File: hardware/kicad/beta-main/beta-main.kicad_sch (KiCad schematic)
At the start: 7 parts

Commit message: add modifications
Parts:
- added J1: AUDIO, Connector_JST:JST_PH_B2B-PH-K_1x02_P2.00mm_Vertical, symbol Connector:Conn_01x02_Socket
- added J2: USB3-0, Connector_JST:JST_PH_B8B-PH-K_1x08_P2.00mm_Vertical, symbol Connector:Conn_01x08_Pin
- added J21: PWR, Connector_JST:JST_PH_B2B-PH-K_1x02_P2.00mm_Vertical, symbol Connector:Conn_01x02_Pin
- added J3, J4, J7: USB3-1, Connector_JST:JST_PH_B8B-PH-K_1x08_P2.00mm_Vertical, symbol Connector:Conn_01x08_Pin
- added J5: DSI, Connector_FFC-FPC:TE_1-84953-5_1x15-1MP_P1.0mm_Horizontal, symbol Connector:Conn_01x15_Socket
- added J6, J9: USB3_A, BETA:22009L012N1, symbol Connector:USB3_A
- added J8: CSI, Connector_FFC-FPC:TE_1-84953-5_1x15-1MP_P1.0mm_Horizontal, symbol Connector:Conn_01x15_Socket
- added MH10, MH11, MH12, MH9: M2.5, MountingHole:MountingHole_2.7mm_Pad, symbol Mechanical:MountingHole_Pad
- added U1: MAX98357A, Package_DFN_QFN:TQFN-16-1EP_3x3mm_P0.5mm_EP1.23x1.23mm, symbol Beta:MAX98357A
- renumbered MH2 to MH3, MH3 to MH5, MH4 to MH7
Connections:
- net GND: now also J2.8 (Pin_8), J21.2 (Pin_2), J3.8 (Pin_8), J5.1 (Pin_1), J5.10 (Pin_10), J5.13 (Pin_13), J5.4 (Pin_4), J5.7 (Pin_7), J8.1 (Pin_1), J8.10 (Pin_10), J8.4 (Pin_4), J8.7 (Pin_7), MH10.1, MH11.1, MH12.1, MH9.1, U1.11 (GND), U1.15 (GND), U1.17 (PAD), U1.3 (GND)
- new net: J1.2 (Pin_2), U1.10 (OUTN)
- new net: J1.1 (Pin_1), U1.9 (OUTP)
- new net: J4.1 (Pin_1), J6.1 (VBUS)
- new net: J4.2 (Pin_2), J6.2 (D-)
- new net: J4.3 (Pin_3), J6.3 (D+)
- new net: J4.4 (Pin_4), J6.5 (SSRX-)
- new net: J4.5 (Pin_5), J6.6 (SSRX+)
- new net: J4.6 (Pin_6), J6.8 (SSTX-)
- new net: J4.7 (Pin_7), J6.9 (SSTX+)
- new net: J4.8 (Pin_8), J6.10 (SHIELD), J6.4 (GND), J6.7 (DRAIN)
- new net: J7.1 (Pin_1), J9.1 (VBUS)
- new net: J7.8 (Pin_8), J9.10 (SHIELD), J9.4 (GND), J9.7 (DRAIN)
- new net: J7.2 (Pin_2), J9.2 (D-)
- new net: J7.3 (Pin_3), J9.3 (D+)
- new net: J7.4 (Pin_4), J9.5 (SSRX-)
- new net: J7.5 (Pin_5), J9.6 (SSRX+)
- new net: J7.6 (Pin_6), J9.8 (SSTX-)
- new net: J7.7 (Pin_7), J9.9 (SSTX+)
- new net +3V3: J5.14 (Pin_14), J5.15 (Pin_15), J8.15 (Pin_15), U1.2 (GAIN_SLOT), U1.4 (~{SD_MODE}), U1.7 (VDD), U1.8 (VDD)
- new net CAM_GPIO0: J8.11 (Pin_11)
- new net CAM_GPIO1: J8.12 (Pin_12)
- new net GPIO/PWR_BUT: J21.1 (Pin_1)
- new net High Speed Serial/USB3-0-D_N: J2.2 (Pin_2)
- new net High Speed Serial/USB3-0-D_P: J2.3 (Pin_3)
- new net High Speed Serial/USB3-0-RX_N: J2.4 (Pin_4)
- new net High Speed Serial/USB3-0-RX_P: J2.5 (Pin_5)
- new net High Speed Serial/USB3-0-TX_N: J2.6 (Pin_6)
- new net High Speed Serial/USB3-0-TX_P: J2.7 (Pin_7)
- new net High Speed Serial/USB3-1-D_N: J3.2 (Pin_2)
- new net High Speed Serial/USB3-1-D_P: J3.3 (Pin_3)
- new net High Speed Serial/USB3-1-RX_N: J3.4 (Pin_4)
- new net High Speed Serial/USB3-1-RX_P: J3.5 (Pin_5)
- new net High Speed Serial/USB3-1-TX_N: J3.6 (Pin_6)
- new net High Speed Serial/USB3-1-TX_P: J3.7 (Pin_7)
- new net I2S0_SCLK: U1.16 (BCLK)
- new net I2S0_SDO: U1.1 (DIN)
- new net I2S0_WS: U1.14 (LRCLK)
- new net MIPI0_C_N: J5.5 (Pin_5)
- new net MIPI0_C_P: J5.6 (Pin_6)
- new net MIPI0_D0_N: J5.8 (Pin_8)
- new net MIPI0_D0_P: J5.9 (Pin_9)
- new net MIPI0_D1_N: J5.2 (Pin_2)
- new net MIPI0_D1_P: J5.3 (Pin_3)
- new net MIPI1_C_N: J8.8 (Pin_8)
- new net MIPI1_C_P: J8.9 (Pin_9)
- new net MIPI1_D0_N: J8.2 (Pin_2)
- new net MIPI1_D0_P: J8.3 (Pin_3)
- new net MIPI1_D1_N: J8.5 (Pin_5)
- new net MIPI1_D1_P: J8.6 (Pin_6)
- new net SCL0: J5.11 (Pin_11)
- new net SCL1: J8.13 (Pin_13)
- new net SDA0: J5.12 (Pin_12)
- new net SDA1: J8.14 (Pin_14)
- new net VBUS: J2.1 (Pin_1), J3.1 (Pin_1)
- no-connect marks 0 -> 8
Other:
- removed sheet CM5
- added sheet GPIO (gpio.kicad_sch)
- added sheet High Speed Serial (high-speed-serial.kicad_sch)
- added sheet Peripherals (peripherals.kicad_sch)
- sheet PSU ports: added VBUS_EN; removed none
- note added: "A_OUT"
- note added: "Audio Interface"
- note added: "BNO"
- note added: "BOARD MOUNT"
- note added: "CSI"
- note added: "DISPLAY MOUNT"
- note added: "DSI"
- note added: "GPIO"
- note added: "HIGH SPEED"
- note added: "MIPI"
- note added: "MISC"
- note added: "SERVO"
- note added: "USB"
- note added: "USB 3.0"
- title: BETA MAIN BOARD -> BETA MAIN BOARD - CM5
- moved on the sheet: FID1, FID2, FID3, MH1, MH3, MH5, MH7

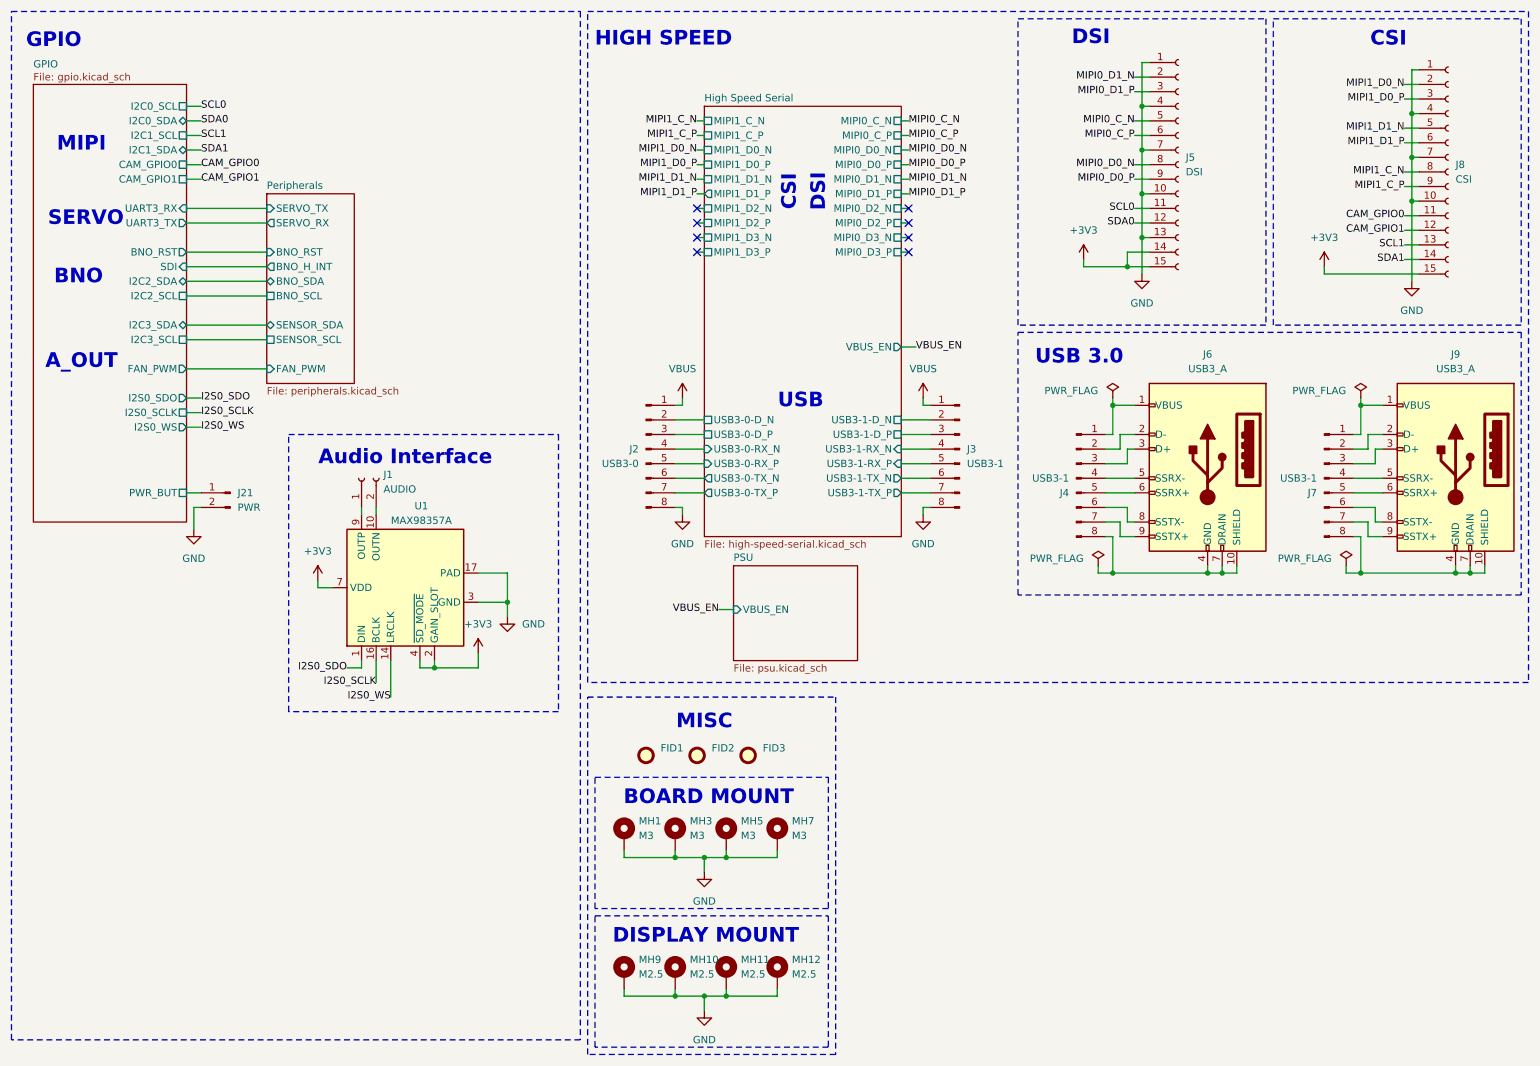
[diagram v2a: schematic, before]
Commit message: BOM, all easily found parts from digi
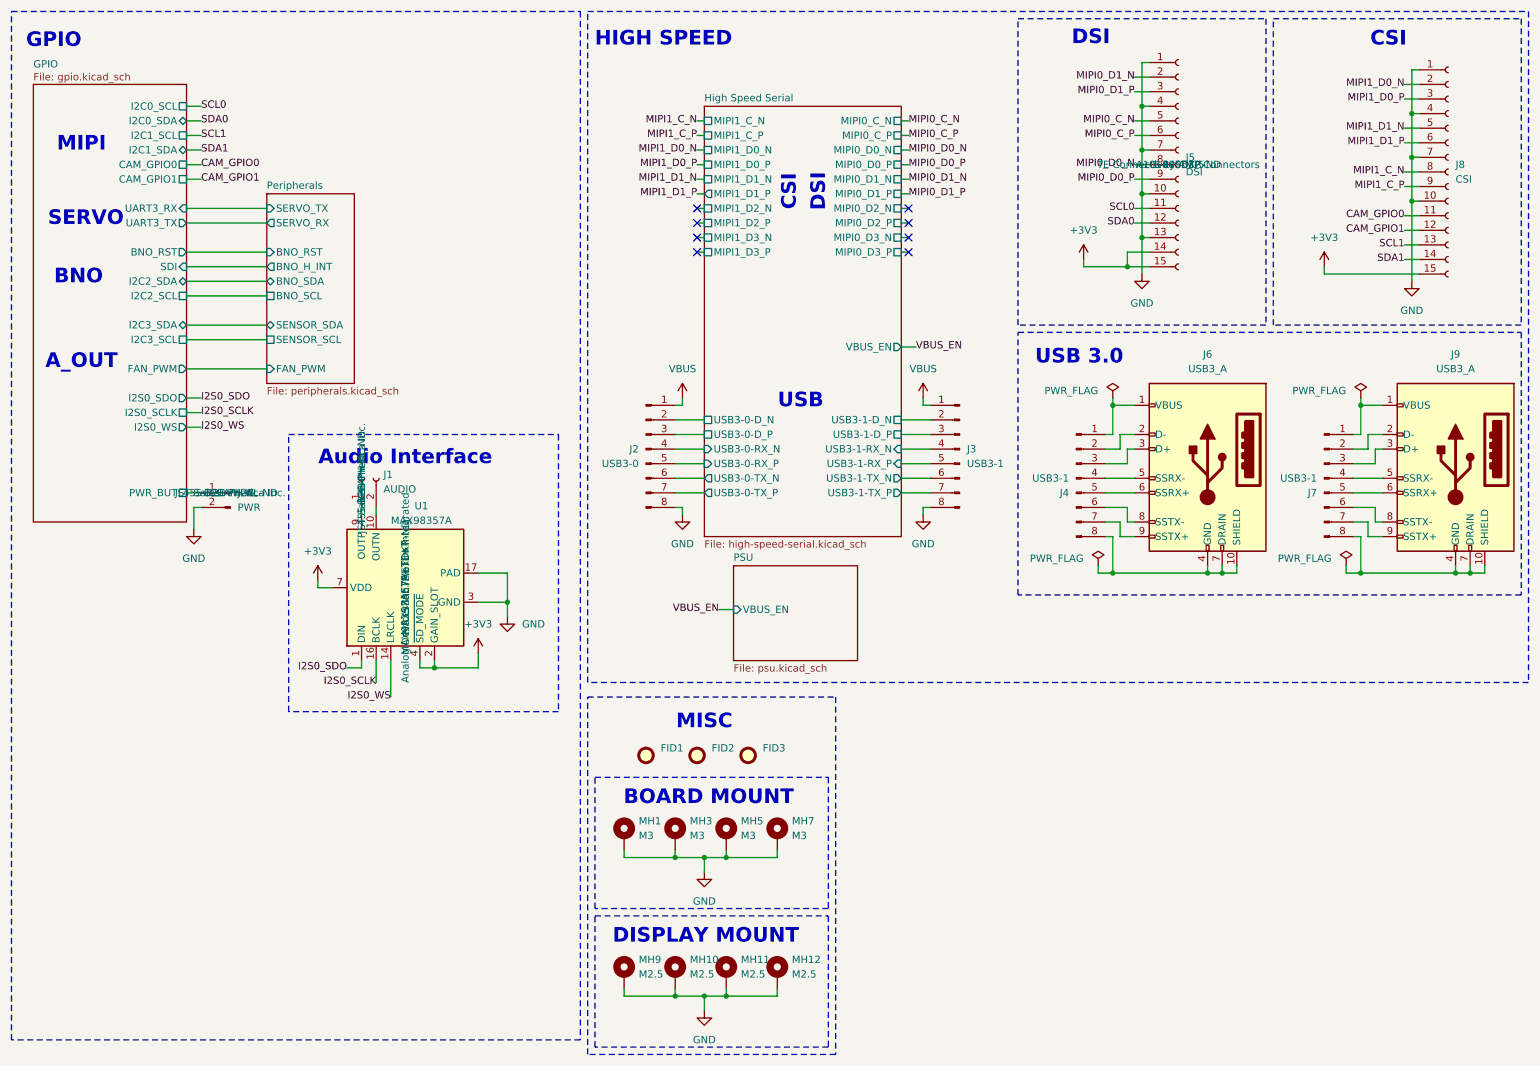
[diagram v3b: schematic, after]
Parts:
- J1, J21: DigiKey_Part_Number (none) -> 455-B2B-PH-KL-ND; MANUFACTURER (none) -> JST Sales America Inc.; MP (none) -> B2B-PH-KL
- J5: DigiKey_Part_Number (none) -> A101405DKR-ND; MANUFACTURER (none) -> TE Connectivity AMP Connectors; MP (none) -> 1-84953-5
- U1: DigiKey_Part_Number (none) -> MAX98357AETE+TDKR-ND; MANUFACTURER (none) -> Analog Devices Inc./Maxim Integrated; MP (none) -> MAX98357AETE+T
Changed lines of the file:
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@@
+			)
+		)
+		(property "DigiKey_Part_Number" "MAX98357AETE+TDKR-ND"
+			(at 81.28 114.3 0)
+			(effects
+				(font
+					(size 1.27 1.27)
+				)
+			)
+		)
+		(property "MANUFACTURER" "Analog Devices Inc./Maxim Integrated"
+			(at 81.28 114.3 0)
+			(effects
+				(font
+					(size 1.27 1.27)
+				)
+			)
+		)
+		(property "MP" "MAX98357AETE+T"
+			(at 81.28 114.3 0)
+			(effects
+				(font
+					(size 1.27 1.27)
+				)
 			)
 		)
@@
 			)
 		)
+		(property "DigiKey_Part_Number" "455-B2B-PH-KL-ND"
+			(at 73.66 95.25 0)
+			(effects
+				(font
+					(size 1.27 1.27)
+				)
+			)
+		)
+		(property "MANUFACTURER" "JST Sales America Inc."
+			(at 73.66 95.25 0)
+			(effects
+				(font
+					(size 1.27 1.27)
+				)
+			)
+		)
+		(property "MP" "B2B-PH-KL"
+			(at 73.66 95.25 0)
+			(effects
+				(font
+					(size 1.27 1.27)
+				)
+			)
+		)
 		(pin "2"
 		)
@@
 			)
 		)
+		(property "DigiKey_Part_Number" "455-B2B-PH-KL-ND"
+			(at 50.8 97.79 0)
+			(effects
+				(font
+					(size 1.27 1.27)
+				)
+			)
+		)
+		(property "MANUFACTURER" "JST Sales America Inc."
+			(at 50.8 97.79 0)
+			(effects
+				(font
+					(size 1.27 1.27)
+				)
+			)
+		)
+		(property "MP" "B2B-PH-KL"
+			(at 50.8 97.79 0)
+			(effects
+				(font
+					(size 1.27 1.27)
+				)
+			)
+		)
 		(pin "2"
 		)
@@
 			)
 		)
+		(property "DigiKey_Part_Number" "A101405DKR-ND"
+			(at 215.9 40.64 0)
+			(effects
+				(font
+					(size 1.27 1.27)
+				)
+			)
+		)
+		(property "MANUFACTURER" "TE Connectivity AMP Connectors"
+			(at 215.9 40.64 0)
+			(effects
+				(font
+					(size 1.27 1.27)
+				)
+			)
+		)
+		(property "MP" "1-84953-5"
+			(at 215.9 40.64 0)
+			(effects
+				(font
+					(size 1.27 1.27)
+				)
+			)
+		)

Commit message: resolve DRC issues and generate fab files
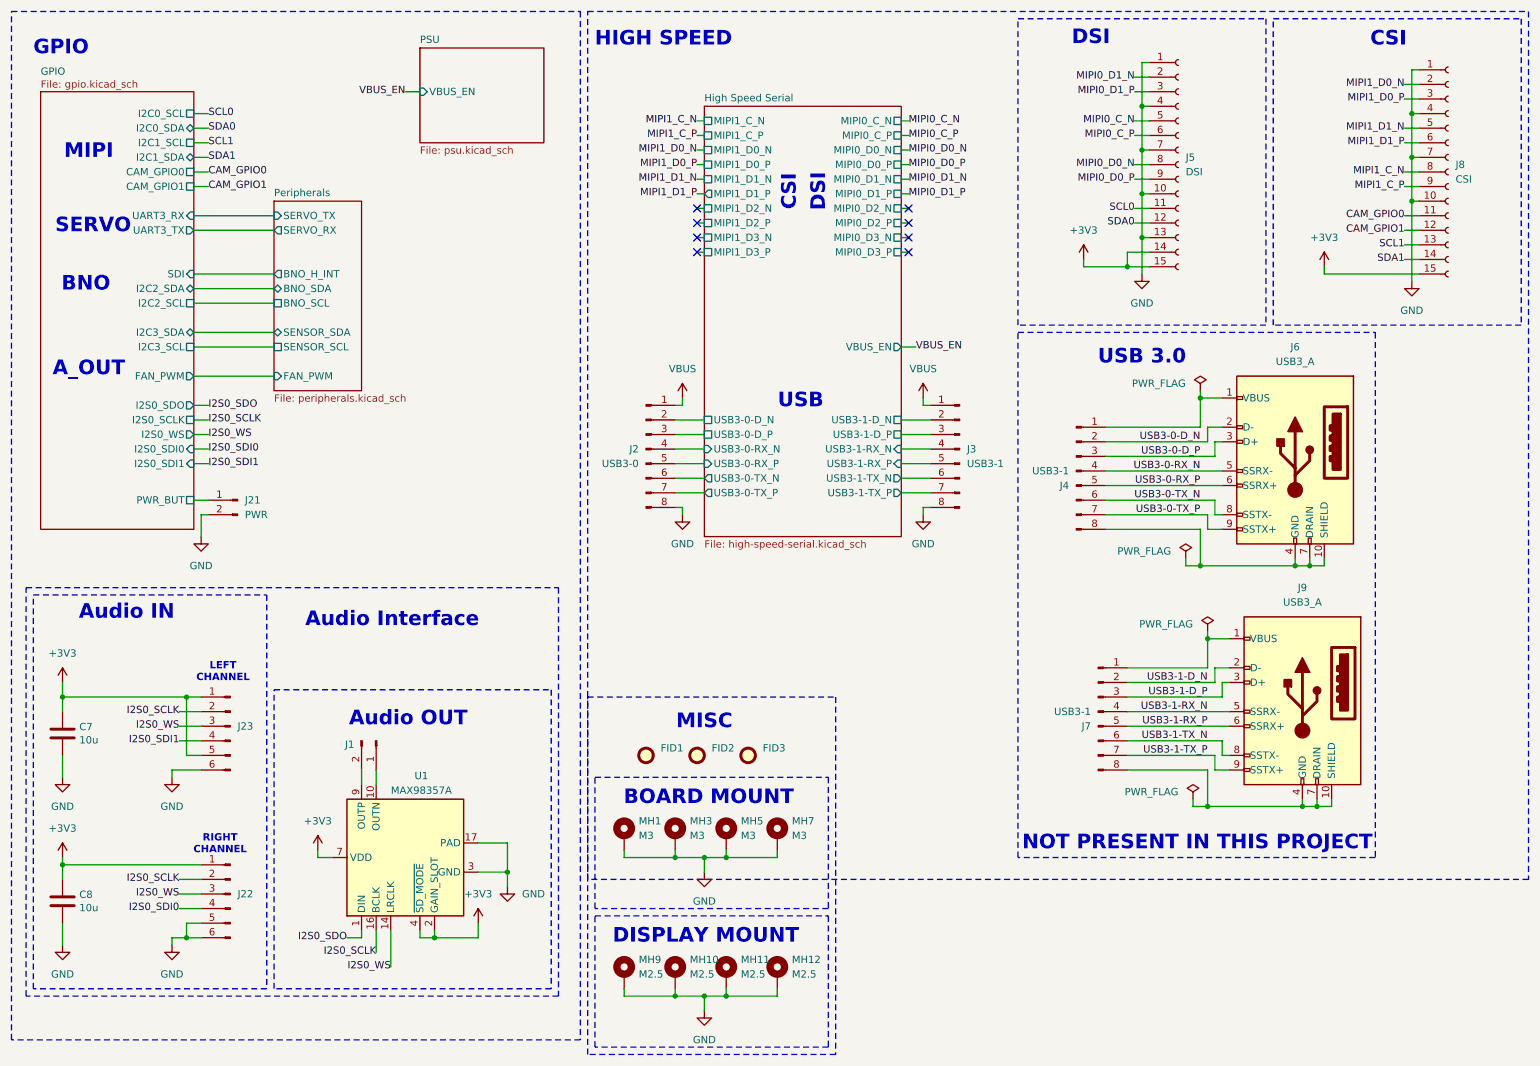
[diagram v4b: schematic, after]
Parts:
- added C7, C8: 10u, Capacitor_SMD:C_0603_1608Metric, symbol Device:C
- added J22: AUDIO_IN0, Connector_JST:JST_PH_B6B-PH-K_1x06_P2.00mm_Vertical, symbol Connector:Conn_01x06_Pin
- added J23: AUDIO_IN1, Connector_JST:JST_PH_B6B-PH-K_1x06_P2.00mm_Vertical, symbol Connector:Conn_01x06_Pin
- J1: symbol Connector:Conn_01x02_Socket -> Connector:Conn_01x02_Pin
- J4, J7: footprint Connector_JST:JST_PH_B8B-PH-K_1x08_P2.00mm_Vertical -> Connector_JST:JST_PH_S8B-PH-K_1x08_P2.00mm_Horizontal; now left out of the parts list
- J6, J9: now left out of the parts list
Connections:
- net +3V3: now also C7.1, C8.1, J22.1 (Pin_1), J23.1 (Pin_1), J23.5 (Pin_5)
- net GND: now also C7.2, C8.2, J22.5 (Pin_5), J22.6 (Pin_6), J23.6 (Pin_6)
- net I2S0_SCLK: now also J22.2 (Pin_2), J23.2 (Pin_2)
- net I2S0_WS: now also J22.3 (Pin_3), J23.3 (Pin_3)
- net at U1.10 (OUTN): now also J1.1 (Pin_1); no longer J1.2 (Pin_2)
- net at U1.9 (OUTP): now also J1.2 (Pin_2); no longer J1.1 (Pin_1)
- net USB3-0-D_N: now reaches J4.2 (Pin_2), J6.2 (D-)
- net USB3-0-D_P: now reaches J4.3 (Pin_3), J6.3 (D+)
- net USB3-0-RX_N: now reaches J4.4 (Pin_4), J6.5 (SSRX-)
- net USB3-0-RX_P: now reaches J4.5 (Pin_5), J6.6 (SSRX+)
- net USB3-0-TX_N: now reaches J4.6 (Pin_6), J6.8 (SSTX-)
- net USB3-0-TX_P: now reaches J4.7 (Pin_7), J6.9 (SSTX+)
- net USB3-1-D_N: now reaches J7.2 (Pin_2), J9.2 (D-)
- net USB3-1-D_P: now reaches J7.3 (Pin_3), J9.3 (D+)
- net USB3-1-RX_N: now reaches J7.4 (Pin_4), J9.5 (SSRX-)
- net USB3-1-RX_P: now reaches J7.5 (Pin_5), J9.6 (SSRX+)
- net USB3-1-TX_N: now reaches J7.6 (Pin_6), J9.8 (SSTX-)
- net USB3-1-TX_P: now reaches J7.7 (Pin_7), J9.9 (SSTX+)
- new net I2S0_SDI0: J22.4 (Pin_4)
- new net I2S0_SDI1: J23.4 (Pin_4)
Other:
- sheet GPIO ports: added I2S0_SDI0, I2S0_SDI1; removed BNO_RST
- sheet Peripherals ports: added none; removed BNO_RST
- note added: "Audio IN"
- note added: "Audio OUT"
- note added: "LEFT CHANNEL"
- note added: "NOT PRESENT IN THIS PROJECT"
- note added: "RIGHT CHANNEL"
- moved on the sheet: J21, J4, J6, J7, J9, U1

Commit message: add final touches, generate rev A fab and step files
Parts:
- added J26: Conn_01x04_Pin, Connector_JST:JST_PH_B4B-PH-K_1x04_P2.00mm_Vertical, symbol Connector:Conn_01x04_Pin
- J1: value AUDIO -> Conn_01x02_Pin; MP B2B-PH-KL -> B2B-PH-K
- J2: value USB3-0 -> Conn_01x08_Pin
- J21: value PWR -> Conn_01x02_Pin
- J22: value AUDIO_IN0 -> Conn_01x06_Pin
- J23: value AUDIO_IN1 -> Conn_01x06_Pin
- J3: value USB3-1 -> Conn_01x08_Pin
- J5: value DSI -> FFC
- J8: value CSI -> FFC
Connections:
- net GND: now also J26.4 (Pin_4)
- net GPIO/I2C3_SCL: now also J26.3 (Pin_3)
- net GPIO/I2C3_SDA: now also J26.2 (Pin_2)
- new net GPIO/BATT_INT: J26.1 (Pin_1)
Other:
- sheet GPIO ports: added BATT_INT; removed none
